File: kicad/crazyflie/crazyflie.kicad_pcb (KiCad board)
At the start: 2 copper layers, 47.6 x 51 mm, 16 parts, among them J1 Conn_01x04_Socket, J2 Conn_01x03_Socket, J3 Conn_01x02_Socket, J4 Conn_01x14_Socket, J5 Conn_01x14_Socket, J6 Conn_01x04_Socket, J7 Conn_01x03_Socket, J8 Conn_01x04_Socket, M1 Conn_01x03_Socket, M2 Conn_01x03_Socket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

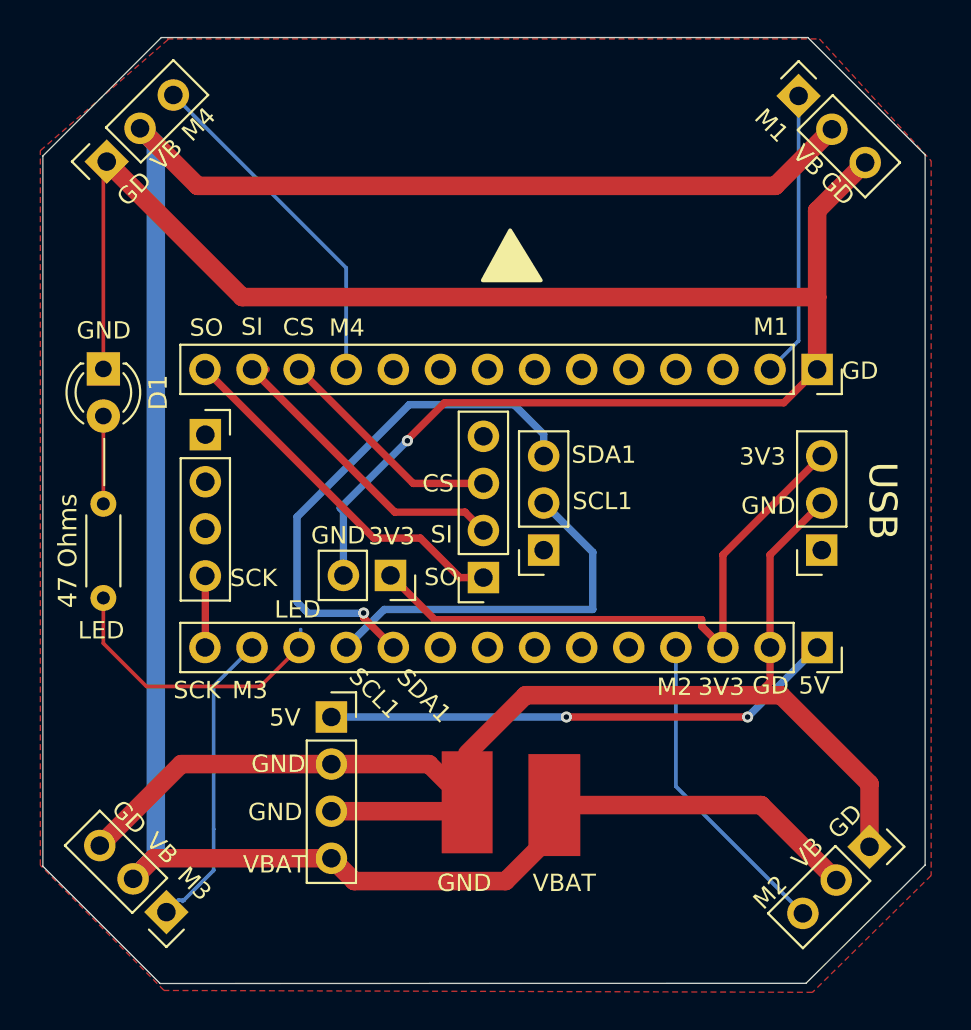
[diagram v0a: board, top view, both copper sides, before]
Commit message: modified:   kicad/crazyflie/crazyflie.kicad_pro
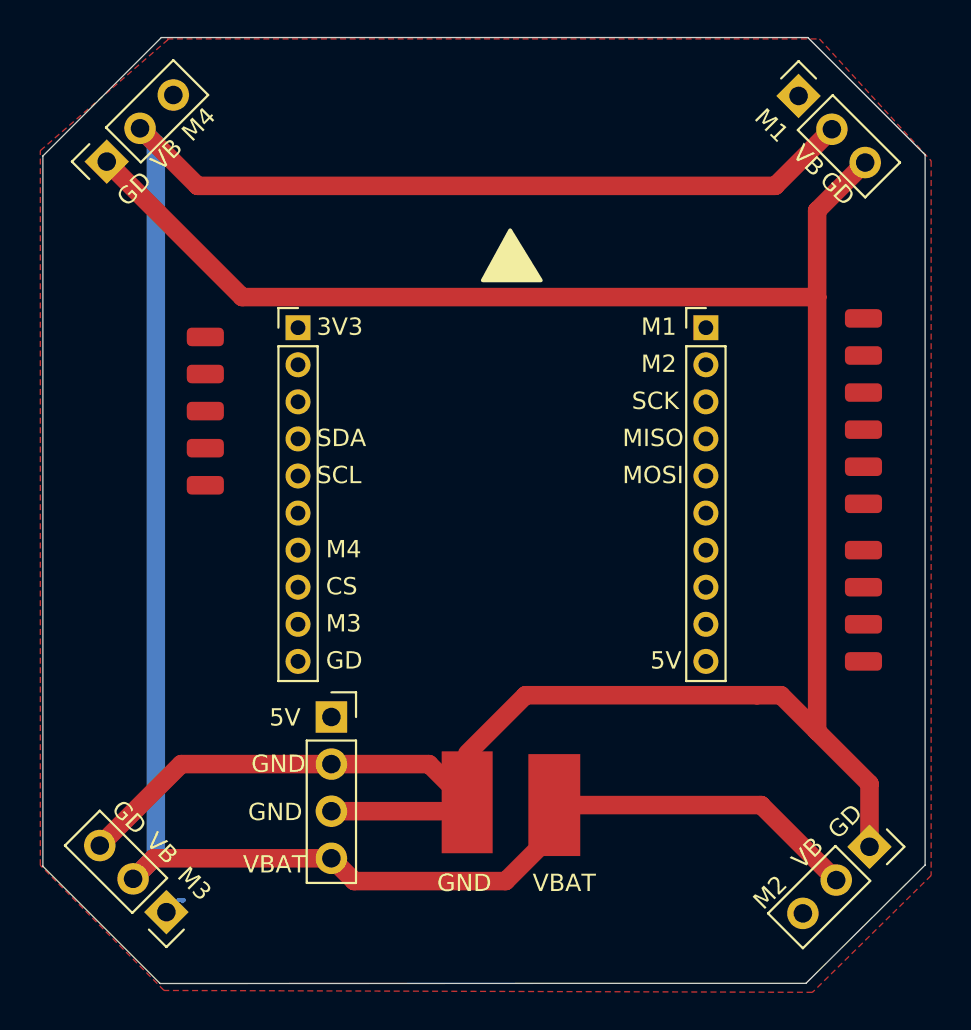
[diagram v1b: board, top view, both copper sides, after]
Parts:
- removed D1: LED, LED_THT:LED_D3.0mm
- removed J3: Conn_01x02_Socket, Connector_PinSocket_2.54mm:PinSocket_1x02_P2.54mm_Vertical
- removed J4, J5: Conn_01x14_Socket, Connector_PinSocket_2.54mm:PinSocket_1x14_P2.54mm_Vertical
- removed J6: Conn_01x04_Socket, Connector_PinSocket_2.54mm:PinSocket_1x04_P2.54mm_Vertical
- removed J7: Conn_01x03_Socket, Connector_PinSocket_2.54mm:PinSocket_1x03_P2.54mm_Vertical
- removed R1: 47 Ohms, Resistor_THT:R_Axial_DIN0204_L3.6mm_D1.6mm_P5.08mm_Horizontal
- added VB_PAD10: Conn_01x01, Connector_Wire:SolderWirePad_1x01_SMD_1x2mm, F.Cu at (135.0, 98.0)
- added VB_PAD11: Conn_01x01, Connector_Wire:SolderWirePad_1x01_SMD_1x2mm, F.Cu at (135.0, 94.0)
- added VB_PAD12: Conn_01x01, Connector_Wire:SolderWirePad_1x01_SMD_1x2mm, F.Cu at (135.0, 96.0)
- added VB_PAD13: Conn_01x01, Connector_Wire:SolderWirePad_1x01_SMD_1x2mm, F.Cu at (170.5, 103.0)
- added VB_PAD14: Conn_01x01, Connector_Wire:SolderWirePad_1x01_SMD_1x2mm, F.Cu at (170.5, 111.5)
- added VB_PAD14: Conn_01x01, Connector_Wire:SolderWirePad_1x01_SMD_1x2mm, F.Cu at (170.5, 109.5)
- added VB_PAD15: Conn_01x01, Connector_Wire:SolderWirePad_1x01_SMD_1x2mm, F.Cu at (170.5, 97.0)
- added VB_PAD2: Conn_01x01, Connector_Wire:SolderWirePad_1x01_SMD_1x2mm, F.Cu at (170.5, 101.0)
- added VB_PAD3: Conn_01x01, Connector_Wire:SolderWirePad_1x01_SMD_1x2mm, F.Cu at (170.5, 105.5)
- added VB_PAD4: Conn_01x01, Connector_Wire:SolderWirePad_1x01_SMD_1x2mm, F.Cu at (170.5, 107.5)
- added VB_PAD5: Conn_01x01, Connector_Wire:SolderWirePad_1x01_SMD_1x2mm, F.Cu at (135.0, 100.0)
- added VB_PAD6: Conn_01x01, Connector_Wire:SolderWirePad_1x01_SMD_1x2mm, F.Cu at (135.0, 102.0)
- added VB_PAD7: Conn_01x01, Connector_Wire:SolderWirePad_1x01_SMD_1x2mm, F.Cu at (170.5, 99.0)
- added VB_PAD8: Conn_01x01, Connector_Wire:SolderWirePad_1x01_SMD_1x2mm, F.Cu at (170.5, 93.0)
- added VB_PAD9: Conn_01x01, Connector_Wire:SolderWirePad_1x01_SMD_1x2mm, F.Cu at (170.5, 95.0)
- J1: value Conn_01x04_Socket -> Conn_01x10_Female; footprint Connector_PinSocket_2.54mm:PinSocket_1x04_P2.54mm_Vertical -> Connector_PinHeader_2.00mm:PinHeader_1x10_P2.00mm_Vertical
- J2: value Conn_01x03_Socket -> Conn_01x10_Female; footprint Connector_PinSocket_2.54mm:PinSocket_1x03_P2.54mm_Vertical -> Connector_PinHeader_2.00mm:PinHeader_1x10_P2.00mm_Vertical
- moved J2 13.5 mm to (162.0, 93.5), turned to 0 degrees
- moved J1 7.63 mm to (140.0, 93.5)
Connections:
- J1 pad 1: unconnected-(J1-Pin_1-Pad1) -> /3V3
- J1 pad 2: unconnected-(J1-Pin_2-Pad2) -> /RX
- J1 pad 3: unconnected-(J1-Pin_3-Pad3) -> /TX
- J1 pad 4: /SCK -> /SDA
- J2 pad 1: unconnected-(J2-Pin_1-Pad1) -> /M1
- J2 pad 2: /GND -> /M2
- J2 pad 3: /3V3 -> /SCK
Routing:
- net /GND: track 172.8 -> 137.0 mm, vias 1 -> 0
- net /3V3: track 32.3 -> 0.00 mm
- net /SDA1: track 28.6 -> 0.00 mm, vias 1 -> 0
- net /5V: track 27.7 -> 0.00 mm, vias 2 -> 0
- net /SCL1: track 21.0 -> 0.00 mm
- net /MISO: track 19.7 -> 0.00 mm
- net /M4: track 19.3 -> 0.00 mm
- net /M2: track 17.4 -> 0.00 mm
- net /MOSI: track 16.8 -> 0.00 mm
- net /LED1: track 15.8 -> 0.00 mm
- net /M1: track 15.4 -> 0.00 mm
- net /M3: track 16.5 -> 1.33 mm
- net /CS: track 12.5 -> 0.00 mm
- net Net-(D1-A): track 4.73 -> 0.00 mm
- net /SCK: track 3.87 -> 0.00 mm
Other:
- board text added: "MISO"
- board text added: "MOSI"
- board text added: "SCL"
- board text added: "SDA"
- board text removed: "LED"
- board text removed: "PMW3901"
- board text removed: "SCL1"
- board text removed: "SDA1"
- board text removed: "SI"
- board text removed: "SO"
- board text removed: "USB"
- board text removed: "VL53L1X"

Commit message: modified:   kicad/crazyflie/crazyflie.kicad_pcb
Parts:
- removed VB_PAD10, VB_PAD11, VB_PAD12, VB_PAD13, VB_PAD14 (x2), VB_PAD15, VB_PAD2, VB_PAD3, VB_PAD4, VB_PAD5, VB_PAD6, VB_PAD7, VB_PAD8, VB_PAD9: Conn_01x01, Connector_Wire:SolderWirePad_1x01_SMD_1x2mm

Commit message: modified:   kicad/crazyflie/crazyflie.kicad_pcb
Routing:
- net /M2: track 0.00 -> 32.6 mm
- net /M4: track 0.00 -> 27.3 mm
- net /5V: track 0.00 -> 21.4 mm
- net /M3: track 1.33 -> 18.5 mm
- net /M1: track 0.00 -> 14.6 mm
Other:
- board text removed: "3V3"
- board text removed: "CS"
- board text removed: "MISO"
- board text removed: "MOSI"
- board text removed: "SCK"
- board text removed: "SCL"
- board text removed: "SDA"
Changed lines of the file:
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@@
-		)
-	)
-	(gr_text "SCK"
-		(at 158 98 0)
-		(layer "F.SilkS")
-		(effects
-			(font
-				(size 0.93472 0.93472)
-				(thickness 0.08128)
-			)
-			(justify left bottom)
 		)
 	)
@@
 		)
 	)
-	(gr_text "MISO"
-		(at 157.5 100 0)
-		(layer "F.SilkS")
-		(effects
-			(font
-				(size 0.93472 0.93472)
-				(thickness 0.08128)
-			)
-			(justify left bottom)
-		)
-	)
-	(gr_text "SCL"
-		(at 141 102 0)
-		(layer "F.SilkS")
-		(effects
-			(font
-				(size 0.93472 0.93472)
-				(thickness 0.08128)
-			)
-			(justify left bottom)
-		)
-	)
 	(gr_text "GD"
 		(at 169.2 121.225 45)
@@
 		)
 	)
-	(gr_text "SDA\n"
-		(at 141 100 0)
-		(layer "F.SilkS")
-		(effects
-			(font
-				(size 0.93472 0.93472)
-				(thickness 0.08128)
-			)
-			(justify left bottom)
-		)
-	)
 	(gr_text "M2"
 		(at 158.5 96 0)
@@
 		)
 	)
-	(gr_text "MOSI"
-		(at 157.5 102 0)
-		(layer "F.SilkS")
-		(effects
-			(font
-				(size 0.93472 0.93472)
-				(thickness 0.08128)
-			)
-			(justify left bottom)
-		)
-	)
 	(gr_text "GND"
 		(at 137.475 117.575 0)
@@
 	(gr_text "VB"
 		(at 166.525 84.25 315)
-		(layer "F.SilkS")
-		(effects
-			(font
-				(size 0.93472 0.93472)
-				(thickness 0.08128)
-			)
-			(justify left bottom)
-		)
-	)
-	(gr_text "3V3"
-		(at 141 94 0)
-		(layer "F.SilkS")
-		(effects
-			(font
-				(size 0.93472 0.93472)
-				(thickness 0.08128)
-			)
-			(justify left bottom)
-		)
-	)
-	(gr_text "CS"
-		(at 141.5 108 0)
 		(layer "F.SilkS")
 		(effects
@@
 		(start 149.125 119.1)
 		(end 149.125 116.475)
-		(width 0.2)
+		(width 1)
 		(layer "F.Cu")
 		(net 1)
@@
 	)
 	(segment
-		(start 133.85 124.375)
-		(end 133.775 124.45)
-		(width 0.2)
+		(start 167 88.5)
+		(end 162 93.5)
+		(width 0.4)
+		(layer "B.Cu")
+		(net 17)
+	)
+	(segment
+		(start 167 81)
+		(end 167 88.5)
+		(width 0.4)
+		(layer "B.Cu")
+		(net 17)
+	)
+	(segment
+		(start 162 95.5)
+		(end 163.371331 95.5)
+		(width 0.4)
+		(layer "B.Cu")
+		(net 18)
+	)
+	(segment
+		(start 164.155751 96.28442)
+		(end 164.155751 122.014955)
+		(width 0.4)
+		(layer "B.Cu")
+		(net 18)
+	)
+	(segment
+		(start 164.155751 122.014955)
+		(end 167.232898 125.092102)
+		(width 0.4)
+		(layer "B.Cu")
+		(net 18)
+	)
+	(segment
+		(start 163.371331 95.5)
+		(end 164.155751 96.28442)
+		(width 0.4)
+		(layer "B.Cu")
+		(net 18)
+	)
+	(segment
+		(start 164.155751 96.250328)
+		(end 164.155751 96.28442)
+		(width 0.4)
+		(layer "B.Cu")
+		(net 18)
+	)
+	(segment
+		(start 135.478362 114.021638)
+		(end 135.478362 122.446638)
+		(width 0.4)
 		(layer "B.Cu")
 		(net 19)
 	)
 	(segment
-		(start 133.85 124.375)
-		(end 133.55 124.375)
-		(width 0.2)
+		(start 135.478362 122.446638)
+		(end 132.9 125.025)
+		(width 0.4)
 		(layer "B.Cu")
 		(net 19)
 	)
 	(segment
-		(start 133.55 124.375)
-		(end 132.9 125.025)
-		(width 0.2)
+		(start 140 109.5)
+		(end 135.478362 114.021638)
+		(width 0.4)
 		(layer "B.Cu")
 		(net 19)
 	)
+	(segment
+		(start 133.275 98.775)
+		(end 140 105.5)
+		(width 0.4)
+		(layer "B.Cu")
+		(net 20)
+	)
+	(segment
+		(start 133.275 80.95)
+		(end 133.275 98.775)
+		(width 0.4)
+		(layer "B.Cu")
+		(net 20)
+	)
+	(segment
+		(start 159 114.5)
+		(end 162 111.5)
+		(width 0.4)
+		(layer "B.Cu")
+		(net 21)
+	)
+	(segment
+		(start 141.8 114.5)
+		(end 159 114.5)
+		(width 0.4)
+		(layer "B.Cu")
+		(net 21)
+	)
 	(zone

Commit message: modified:   kicad/crazyflie/crazyflie.kicad_pcb
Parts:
- added H1: MountingHole, MountingHole:MountingHole_5.3mm_M5_ISO7380_Pad_TopOnly, F.Cu at (135.4, 89.7)
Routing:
- net /VBAT: track 124.3 -> 168.7 mm
- net /GND: track 137.0 -> 131.4 mm
- net /M4: track 27.3 -> 31.7 mm
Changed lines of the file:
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@@
 			)
 		)
-		(property "Datasheet" "~"
+		(property "Datasheet" ""
 			(at 0 0 45)
 			(layer "F.Fab")
@@
 			)
 		)
-		(property "Datasheet" "~"
+		(property "Datasheet" ""
 			(at 0 0 135)
 			(layer "F.Fab")
@@
 			)
 		)
+	)
+	(footprint "MountingHole:MountingHole_5.3mm_M5_ISO7380_Pad_TopOnly"
+		(layer "F.Cu")
+		(at 135.425 89.65)
+		(descr "Mounting Hole 5.3mm, M5, generated by kicad-footprint-generator mountinghole.py")
+		(tags "mountinghole M5 ISO7380")
+		(property "Reference" "H1"
+			(at 0 -5.7 0)
+			(layer "F.SilkS")
+			(hide yes)
+			(effects
+				(font
+					(size 1 1)
+					(thickness 0.15)
+				)
+			)
+		)
+		(property "Value" "MountingHole"
+			(at 0 5.7 0)
+			(layer "F.Fab")
+			(hide yes)
+			(effects
+				(font
+					(size 1 1)
+					(thickness 0.15)
+				)
+			)
+		)
+		(property "Datasheet" ""
+			(at 0 0 0)
+			(layer "F.Fab")
+			(hide yes)
+			(effects
+				(font
+					(size 1.27 1.27)
+					(thickness 0.15)
+				)
+			)
+		)
+		(property "Description" "Mounting Hole without connection"
+			(at 0 0 0)
+			(layer "F.Fab")
+			(hide yes)
+			(effects
+				(font
+					(size 1.27 1.27)
+					(thickness 0.15)
+				)
+			)
+		)
+		(property ki_fp_filters "MountingHole*")
+		(sheetname "/")
+		(sheetfile "crazyflie.kicad_sch")
+		(attr exclude_from_pos_files exclude_from_bom)
+		(pad "1" thru_hole circle
+			(at 0 -0.65)
+			(size 5.7 5.7)
+			(drill 5.3)
+			(layers "*.Cu" "*.Mask")
+			(remove_unused_layers no)
+			(zone_connect 2)
+		)
+		(embedded_fonts no)
 	)
 	(footprint "Connector_Wire:SolderWirePad_1x01_SMD_5x10mm"
@@
 			)
 		)
-		(property "Datasheet" "~"
+		(property "Datasheet" ""
 			(at 0 0 0)
 			(layer "F.Fab")
@@
 			)
 		)
-		(property "Datasheet" "~"
+		(property "Datasheet" ""
 			(at 0 0 135)
 			(layer "F.Fab")
@@
 			)
 		)
-		(property "Datasheet" "~"
+		(property "Datasheet" ""
 			(at 0 0 0)
 			(layer "F.Fab")
@@
 			)
 		)
-		(property "Datasheet" "~"
+		(property "Datasheet" ""
 			(at 0 0 0)
 			(layer "F.Fab")
@@
 			)
 		)
-		(property "Datasheet" "~"
+		(property "Datasheet" ""
 			(at 0 0 45)
 			(layer "F.Fab")
@@
 	)
 	(segment
-		(start 168 91.85)
-		(end 136.990796 91.85)
+		(start 129.682898 84.542102)
+		(end 129.682898 109.097898)
 		(width 1)
 		(layer "F.Cu")
@@
 	(segment
 		(start 133.700796 117.04)
-		(end 141.8 117.04)
+		(end 137.625 117.04)
 		(width 1)
 		(layer "F.Cu")
@@
 	)
 	(segment
+		(start 129.682898 109.097898)
+		(end 137.625 117.04)
+		(width 1)
+		(layer "F.Cu")
+		(net 1)
+	)
+	(segment
 		(start 141.8 119.58)
 		(end 148.645 119.58)
@@
 	)
 	(segment
-		(start 136.990796 91.85)
-		(end 129.682898 84.542102)
+		(start 137.625 117.04)
+		(end 141.8 117.04)
 		(width 1)
 		(layer "F.Cu")
@@
 	)
 	(segment
-		(start 165.742102 85.85)
-		(end 168.796051 82.796051)
-		(width 1)
-		(layer "F.Cu")
-		(net 16)
-	)
-	(segment
 		(start 132.212898 122.12)
 		(end 141.8 122.12)
@@
 	)
 	(segment
-		(start 131.478949 82.746051)
-		(end 134.582898 85.85)
-		(width 1)
-		(layer "F.Cu")
-		(net 16)
-	)
-	(segment
 		(start 153.825 119.25)
 		(end 164.982898 119.25)
-		(width 1)
-		(layer "F.Cu")
-		(net 16)
-	)
-	(segment
-		(start 134.582898 85.85)
-		(end 165.742102 85.85)
 		(width 1)
 		(layer "F.Cu")
@@
 	)
 	(segment
-		(start 132.328949 83.596051)
-		(end 132.328949 122.003949)
+		(start 131.9216 86.9784)
+		(end 128.725 90.175)
 		(width 1)
 		(layer "B.Cu")
@@
 	(segment
 		(start 131.478949 82.746051)
+		(end 132.232898 83.5)
+		(width 1)
+		(layer "B.Cu")
+		(net 16)
+	)
+	(segment
+		(start 131.103949 92.553949)
+		(end 131.103949 123.228949)
+		(width 1)
+		(layer "B.Cu")
+		(net 16)
+	)
+	(segment
+		(start 131.9216 122.411298)
+		(end 131.103949 123.228949)
+		(width 1)
+		(layer "B.Cu")
+		(net 16)
+	)
+	(segment
+		(start 128.725 90.175)
+		(end 131.103949 92.553949)
+		(width 1)
+		(layer "B.Cu")
+		(net 16)
+	)
+	(segment
+		(start 168.092102 83.5)
+		(end 168.796051 82.796051)
+		(width 1)
+		(layer "B.Cu")
+		(net 16)
+	)
+	(segment
+		(start 168.796051 123.063153)
+		(end 169.028949 123.296051)
+		(width 1)
+		(layer "B.Cu")
+		(net 16)
+	)
+	(segment
+		(start 168.796051 82.796051)
+		(end 168.796051 123.063153)
+		(width 1)
+		(layer "B.Cu")
+		(net 16)
+	)
+	(segment
+		(start 131.9216 83.188702)
+		(end 131.9216 86.9784)
+		(width 1)
+		(layer "B.Cu")
+		(net 16)
+	)
+	(segment
+		(start 132.232898 83.5)
+		(end 168.092102 83.5)
+		(width 1)
+		(layer "B.Cu")
+		(net 16)
+	)
+	(segment
+		(start 131.478949 82.746051)
 		(end 132.328949 83.596051)
+		(width 1)
+		(layer "B.Cu")
+		(net 16)
+	)
+	(segment
+		(start 131.478949 82.746051)
+		(end 131.9216 83.188702)
 		(width 1)
 		(layer "B.Cu")
@@
 		(end 162 93.5)
 		(width 0.4)
-		(layer "B.Cu")
+		(layer "F.Cu")
 		(net 17)
 	)
@@
 		(end 167 88.5)
 		(width 0.4)
-		(layer "B.Cu")
+		(layer "F.Cu")
 		(net 17)
 	)
@@
 	)
 	(segment
-		(start 133.275 98.775)
+		(start 133.275 80.95)
+		(end 143.925 91.6)
+		(width 0.4)
+		(layer "F.Cu")
+		(net 20)
+	)
+	(segment
+		(start 141.9 105.5)
 		(end 140 105.5)
 		(width 0.4)
-		(layer "B.Cu")
+		(layer "F.Cu")
 		(net 20)
 	)
 	(segment
-		(start 133.275 80.95)
-		(end 133.275 98.775)
+		(start 143.925 91.6)
+		(end 143.925 103.475)
 		(width 0.4)
-		(layer "B.Cu")
+		(layer "F.Cu")
+		(net 20)
+	)
+	(segment
+		(start 143.925 103.475)
+		(end 141.9 105.5)
+		(width 0.4)
+		(layer "F.Cu")
 		(net 20)
 	)
@@
 		(polygon
 			(pts
-				(xy 132.95 77.925) (xy 168.125 77.925) (xy 174.15 84.5) (xy 174.15 123.05) (xy 167.75 129.35) (xy 132.775 129.25)
-				(xy 126.1 122.5) (xy 126.1 83.95) (xy 133 77.95) (xy 132.975 77.95)
-			)
-		)
+				(xy 132.55 77.825) (xy 167.875 77.925) (xy 174.3 84.45) (xy 174.025 122.95) (xy 167.475 129.375)
+				(xy 132.35 129.275) (xy 125.925 122.25) (xy 126.125 83.775)
+			)
+		)

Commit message: modified:   kicad/crazyflie/crazyflie.kicad_pcb
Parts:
- removed H1: MountingHole, MountingHole:MountingHole_5.3mm_M5_ISO7380_Pad_TopOnly
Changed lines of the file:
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@@
 			)
 		)
-		(property "Datasheet" ""
+		(property "Datasheet" "~"
 			(at 0 0 45)
 			(layer "F.Fab")
@@
 			)
 		)
-		(property "Datasheet" ""
+		(property "Datasheet" "~"
 			(at 0 0 135)
 			(layer "F.Fab")
@@
 			)
 		)
-	)
-	(footprint "MountingHole:MountingHole_5.3mm_M5_ISO7380_Pad_TopOnly"
-		(layer "F.Cu")
-		(at 135.425 89.65)
-		(descr "Mounting Hole 5.3mm, M5, generated by kicad-footprint-generator mountinghole.py")
-		(tags "mountinghole M5 ISO7380")
-		(property "Reference" "H1"
-			(at 0 -5.7 0)
-			(layer "F.SilkS")
-			(hide yes)
-			(effects
-				(font
-					(size 1 1)
-					(thickness 0.15)
-				)
-			)
-		)
-		(property "Value" "MountingHole"
-			(at 0 5.7 0)
-			(layer "F.Fab")
-			(hide yes)
-			(effects
-				(font
-					(size 1 1)
-					(thickness 0.15)
-				)
-			)
-		)
-		(property "Datasheet" ""
-			(at 0 0 0)
-			(layer "F.Fab")
-			(hide yes)
-			(effects
-				(font
-					(size 1.27 1.27)
-					(thickness 0.15)
-				)
-			)
-		)
-		(property "Description" "Mounting Hole without connection"
-			(at 0 0 0)
-			(layer "F.Fab")
-			(hide yes)
-			(effects
-				(font
-					(size 1.27 1.27)
-					(thickness 0.15)
-				)
-			)
-		)
-		(property ki_fp_filters "MountingHole*")
-		(sheetname "/")
-		(sheetfile "crazyflie.kicad_sch")
-		(attr exclude_from_pos_files exclude_from_bom)
-		(pad "1" thru_hole circle
-			(at 0 -0.65)
-			(size 5.7 5.7)
-			(drill 5.3)
-			(layers "*.Cu" "*.Mask")
-			(remove_unused_layers no)
-			(zone_connect 2)
-		)
-		(embedded_fonts no)
 	)
 	(footprint "Connector_Wire:SolderWirePad_1x01_SMD_5x10mm"
@@
 			)
 		)
-		(property "Datasheet" ""
+		(property "Datasheet" "~"
 			(at 0 0 0)
 			(layer "F.Fab")
@@
 			)
 		)
-		(property "Datasheet" ""
+		(property "Datasheet" "~"
 			(at 0 0 135)
 			(layer "F.Fab")
@@
 			)
 		)
-		(property "Datasheet" ""
+		(property "Datasheet" "~"
 			(at 0 0 0)
 			(layer "F.Fab")
@@
 			)
 		)
-		(property "Datasheet" ""
+		(property "Datasheet" "~"
 			(at 0 0 0)
 			(layer "F.Fab")
@@
 			)
 		)
-		(property "Datasheet" ""
+		(property "Datasheet" "~"
 			(at 0 0 45)
 			(layer "F.Fab")
